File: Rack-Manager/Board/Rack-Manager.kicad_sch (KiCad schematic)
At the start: 0 parts

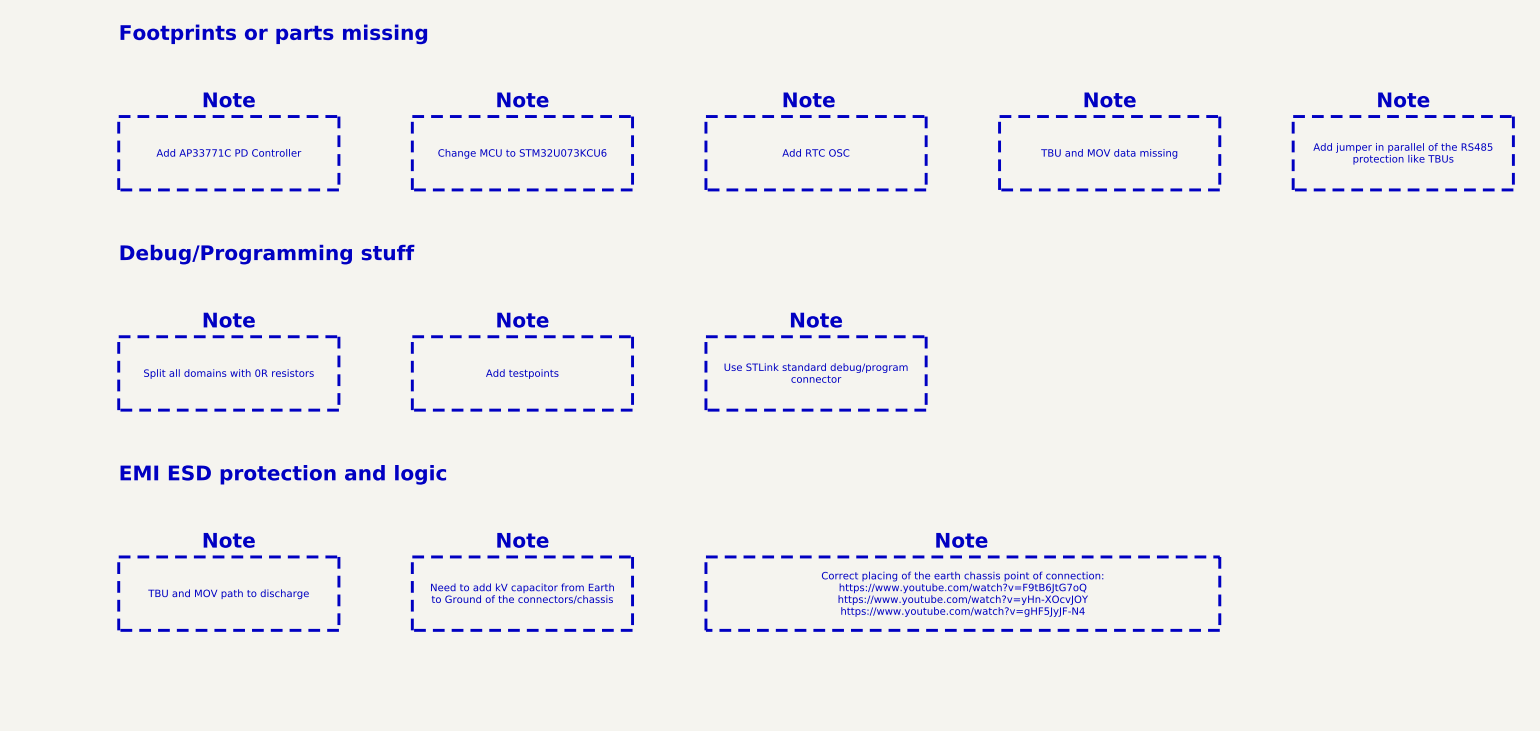
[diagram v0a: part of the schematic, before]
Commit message: Updated .gitignore, added USB-C sink controller and fix earth on GDT
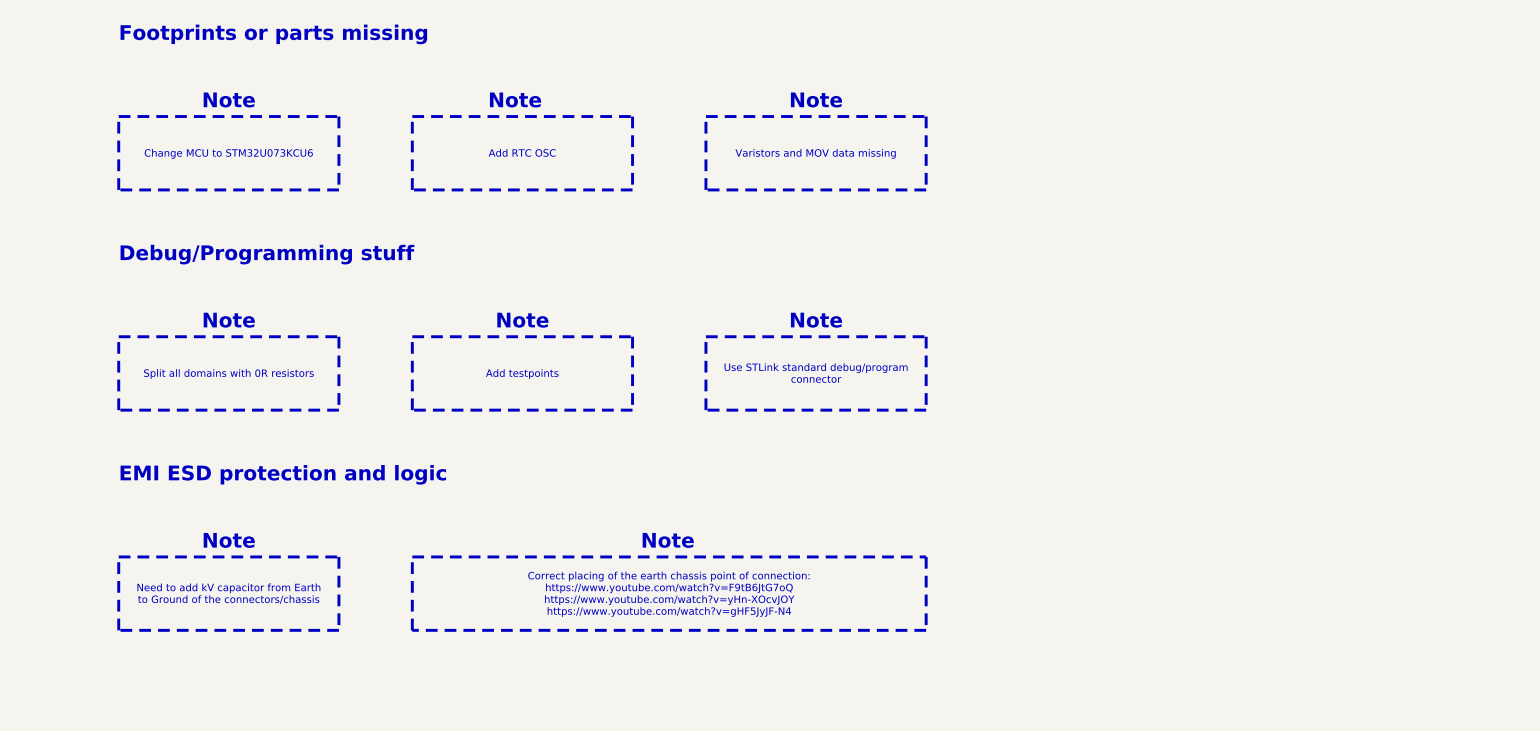
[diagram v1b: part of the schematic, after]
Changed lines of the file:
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@@
 	(text "Note"
 		(exclude_from_sim no)
-		(at 436.88 48.26 0)
-		(effects
-			(font
-				(size 2.54 2.54)
-				(thickness 0.508)
-				(bold yes)
-				(color 194 0 0 1)
-			)
-		)
-	)
-	(text "Note"
-		(exclude_from_sim no)
-		(at 387.35 124.46 0)
+		(at 386.08 48.26 0)
+		(effects
+			(font
+				(size 2.54 2.54)
+				(thickness 0.508)
+				(bold yes)
+				(color 194 0 0 1)
+			)
+		)
+	)
+	(text "Note"
+		(exclude_from_sim no)
+		(at 336.55 124.46 0)
 		(effects
 			(font
@@
 	(text "Note"
 		(exclude_from_sim no)
-		(at 488.95 48.26 0)
-		(effects
-			(font
-				(size 2.54 2.54)
-				(thickness 0.508)
-				(bold yes)
-				(color 194 0 0 1)
-			)
-		)
-	)
-	(text "Note"
-		(exclude_from_sim no)
-		(at 336.55 124.46 0)
-		(effects
-			(font
-				(size 2.54 2.54)
-				(thickness 0.508)
-				(bold yes)
-				(color 194 0 0 1)
-			)
-		)
-	)
-	(text "Note"
-		(exclude_from_sim no)
-		(at 463.296 124.46 0)
+		(at 438.15 48.26 0)
+		(effects
+			(font
+				(size 2.54 2.54)
+				(thickness 0.508)
+				(bold yes)
+				(color 194 0 0 1)
+			)
+		)
+	)
+	(text "Note"
+		(exclude_from_sim no)
+		(at 412.496 124.46 0)
 		(effects
 			(font
@@
 	(text "Note"
 		(exclude_from_sim no)
-		(at 539.75 48.26 0)
-		(effects
-			(font
-				(size 2.54 2.54)
-				(thickness 0.508)
-				(bold yes)
-				(color 194 0 0 1)
-			)
-		)
-	)
-	(text "Note"
-		(exclude_from_sim no)
 		(at 438.15 86.36 0)
 		(effects
@@
 	(text "Note"
 		(exclude_from_sim no)
-		(at 387.35 48.26 0)
-		(effects
-			(font
-				(size 2.54 2.54)
-				(thickness 0.508)
-				(bold yes)
-				(color 194 0 0 1)
-			)
-		)
-	)
-	(text "Note"
-		(exclude_from_sim no)
 		(at 387.35 86.36 0)
 		(effects
@@
 	(text_box "Need to add kV capacitor from Earth to Ground of the connectors/chassis"
 		(exclude_from_sim no)
+		(at 317.5 127 0)
+		(size 38.1 12.7)
+		(margins 0.9525 0.9525 0.9525 0.9525)
+		(stroke
+			(width 0.508)
+			(type dot)
+			(color 194 0 0 1)
+		)
+		(fill
+			(type color)
+			(color 255 165 169 1)
+		)
+		(effects
+			(font
+				(size 1.27 1.27)
+			)
+		)
+	)
+	(text_box "Split all domains with 0R resistors"
+		(exclude_from_sim no)
+		(at 317.5 88.9 0)
+		(size 38.1 12.7)
+		(margins 0.9525 0.9525 0.9525 0.9525)
+		(stroke
+			(width 0.508)
+			(type dot)
+			(color 194 0 0 1)
+		)
+		(fill
+			(type color)
+			(color 255 165 169 1)
+		)
+		(effects
+			(font
+				(size 1.27 1.27)
+			)
+		)
+	)
+	(text_box "Change MCU to STM32U073KCU6"
+		(exclude_from_sim no)
+		(at 317.5 50.8 0)
+		(size 38.1 12.7)
+		(margins 0.9525 0.9525 0.9525 0.9525)
+		(stroke
+			(width 0.508)
+			(type dot)
+			(color 194 0 0 1)
+		)
+		(fill
+			(type color)
+			(color 255 165 169 1)
+		)
+		(effects
+			(font
+				(size 1.27 1.27)
+			)
+		)
+	)
+	(text_box "Varistors and MOV data missing"
+		(exclude_from_sim no)
+		(at 419.1 50.8 0)
+		(size 38.1 12.7)
+		(margins 0.9525 0.9525 0.9525 0.9525)
+		(stroke
+			(width 0.508)
+			(type dot)
+			(color 194 0 0 1)
+		)
+		(fill
+			(type color)
+			(color 255 165 169 1)
+		)
+		(effects
+			(font
+				(size 1.27 1.27)
+			)
+		)
+	)
+	(text_box "Add RTC OSC"
+		(exclude_from_sim no)
+		(at 368.3 50.8 0)
+		(size 38.1 12.7)
+		(margins 0.9525 0.9525 0.9525 0.9525)
+		(stroke
+			(width 0.508)
+			(type dot)
+			(color 194 0 0 1)
+		)
+		(fill
+			(type color)
+			(color 255 165 169 1)
+		)
+		(effects
+			(font
+				(size 1.27 1.27)
+			)
+		)
+	)
+	(text_box "Use STLink standard debug/program connector"
+		(exclude_from_sim no)
+		(at 419.1 88.9 0)
+		(size 38.1 12.7)
+		(margins 0.9525 0.9525 0.9525 0.9525)
+		(stroke
+			(width 0.508)
+			(type dot)
+			(color 194 0 0 1)
+		)
+		(fill
+			(type color)
+			(color 255 165 169 1)
+		)
+		(effects
+			(font
+				(size 1.27 1.27)
+			)
+		)
+	)
+	(text_box "Add testpoints"
+		(exclude_from_sim no)
+		(at 368.3 88.9 0)
+		(size 38.1 12.7)
+		(margins 0.9525 0.9525 0.9525 0.9525)
+		(stroke
+			(width 0.508)
+			(type dot)
+			(color 194 0 0 1)
+		)
+		(fill
+			(type color)
+			(color 255 165 169 1)
+		)
+		(effects
+			(font
+				(size 1.27 1.27)
+			)
+		)
+	)
+	(text_box "Correct placing of the earth chassis point of connection:\nhttps://www.youtube.com/watch?v=F9tB6JtG7oQ\nhttps://www.youtube.com/watch?v=yHn-XOcvJOY\nhttps://www.youtube.com/watch?v=gHF5JyJF-N4"
+		(exclude_from_sim no)
 		(at 368.3 127 0)
-		(size 38.1 12.7)
-		(margins 0.9525 0.9525 0.9525 0.9525)
-		(stroke
-			(width 0.508)
-			(type dot)
-			(color 194 0 0 1)
-		)
-		(fill
-			(type color)
-			(color 255 165 169 1)
-		)
-		(effects
-			(font
-				(size 1.27 1.27)
-			)
-		)
-	)
-	(text_box "Add jumper in parallel of the RS485 protection like TBUs"
-		(exclude_from_sim no)
-		(at 520.7 50.8 0)
-		(size 38.1 12.7)
-		(margins 0.9525 0.9525 0.9525 0.9525)
-		(stroke
-			(width 0.508)
-			(type dot)
-			(color 194 0 0 1)
-		)
-		(fill
-			(type color)
-			(color 255 165 169 1)
-		)
-		(effects
-			(font
-				(size 1.27 1.27)
-			)
-		)
-	)
-	(text_box "Split all domains with 0R resistors"
-		(exclude_from_sim no)
-		(at 317.5 88.9 0)
-		(size 38.1 12.7)
-		(margins 0.9525 0.9525 0.9525 0.9525)
-		(stroke
-			(width 0.508)
-			(type dot)
-			(color 194 0 0 1)
-		)
-		(fill
-			(type color)
-			(color 255 165 169 1)
-		)
-		(effects
-			(font
-				(size 1.27 1.27)
-			)
-		)
-	)
-	(text_box "Change MCU to STM32U073KCU6"
-		(exclude_from_sim no)
-		(at 368.3 50.8 0)
-		(size 38.1 12.7)
-		(margins 0.9525 0.9525 0.9525 0.9525)
-		(stroke
-			(width 0.508)
-			(type dot)
-			(color 194 0 0 1)
-		)
-		(fill
-			(type color)
-			(color 255 165 169 1)
-		)
-		(effects
-			(font
-				(size 1.27 1.27)
-			)
-		)
-	)
-	(text_box "TBU and MOV path to discharge"
-		(exclude_from_sim no)
-		(at 317.5 127 0)
-		(size 38.1 12.7)
-		(margins 0.9525 0.9525 0.9525 0.9525)
-		(stroke
-			(width 0.508)
-			(type dot)
-			(color 194 0 0 1)
-		)
-		(fill
-			(type color)
-			(color 255 165 169 1)
-		)
-		(effects
-			(font
-				(size 1.27 1.27)
-			)
-		)
-	)
-	(text_box "TBU and MOV data missing"
-		(exclude_from_sim no)
-		(at 469.9 50.8 0)
-		(size 38.1 12.7)
-		(margins 0.9525 0.9525 0.9525 0.9525)
-		(stroke
-			(width 0.508)
-			(type dot)
-			(color 194 0 0 1)
-		)
-		(fill
-			(type color)
-			(color 255 165 169 1)
-		)
-		(effects
-			(font
-				(size 1.27 1.27)
-			)
-		)
-	)
-	(text_box "Add RTC OSC"
-		(exclude_from_sim no)
-		(at 419.1 50.8 0)
-		(size 38.1 12.7)
-		(margins 0.9525 0.9525 0.9525 0.9525)
-		(stroke
-			(width 0.508)
-			(type dot)
-			(color 194 0 0 1)
-		)
-		(fill
-			(type color)
-			(color 255 165 169 1)
-		)
-		(effects
-			(font
-				(size 1.27 1.27)
-			)
-		)
-	)
-	(text_box "Add AP33771C PD Controller"
-		(exclude_from_sim no)
-		(at 317.5 50.8 0)
-		(size 38.1 12.7)
-		(margins 0.9525 0.9525 0.9525 0.9525)
-		(stroke
-			(width 0.508)
-			(type dot)
-			(color 194 0 0 1)
-		)
-		(fill
-			(type color)
-			(color 255 165 169 1)
-		)
-		(effects
-			(font
-				(size 1.27 1.27)
-			)
-		)
-	)
-	(text_box "Use STLink standard debug/program connector"
-		(exclude_from_sim no)
-		(at 419.1 88.9 0)
-		(size 38.1 12.7)
-		(margins 0.9525 0.9525 0.9525 0.9525)
-		(stroke
-			(width 0.508)
-			(type dot)
-			(color 194 0 0 1)
-		)
-		(fill
-			(type color)
-			(color 255 165 169 1)
-		)
-		(effects
-			(font
-				(size 1.27 1.27)
-			)
-		)
-	)
-	(text_box "Add testpoints"
-		(exclude_from_sim no)
-		(at 368.3 88.9 0)
-		(size 38.1 12.7)
-		(margins 0.9525 0.9525 0.9525 0.9525)
-		(stroke
-			(width 0.508)
-			(type dot)
-			(color 194 0 0 1)
-		)
-		(fill
-			(type color)
-			(color 255 165 169 1)
-		)
-		(effects
-			(font
-				(size 1.27 1.27)
-			)
-		)
-	)
-	(text_box "Correct placing of the earth chassis point of connection:\nhttps://www.youtube.com/watch?v=F9tB6JtG7oQ\nhttps://www.youtube.com/watch?v=yHn-XOcvJOY\nhttps://www.youtube.com/watch?v=gHF5JyJF-N4"
-		(exclude_from_sim no)
-		(at 419.1 127 0)
 		(size 88.9 12.7)
 		(margins 0.9525 0.9525 0.9525 0.9525)

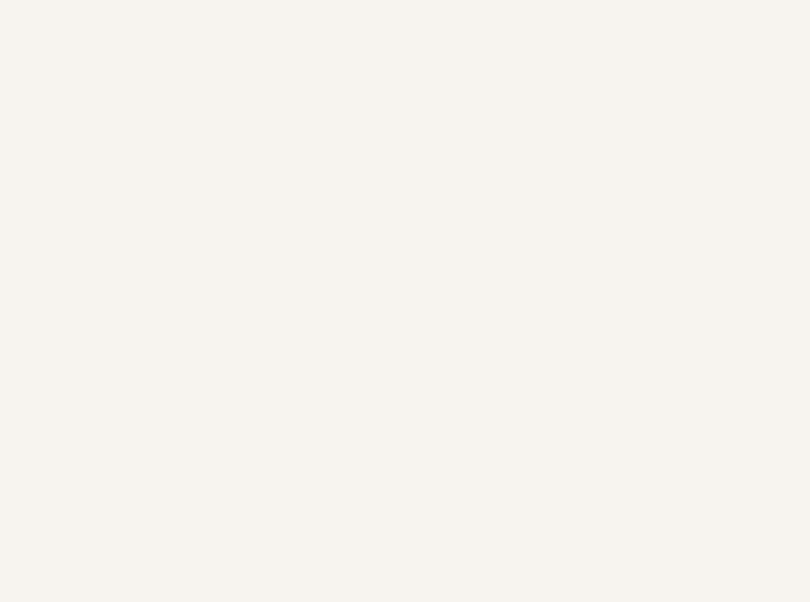
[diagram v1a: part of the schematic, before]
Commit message: Added the fan management sheet and the mosfets for it
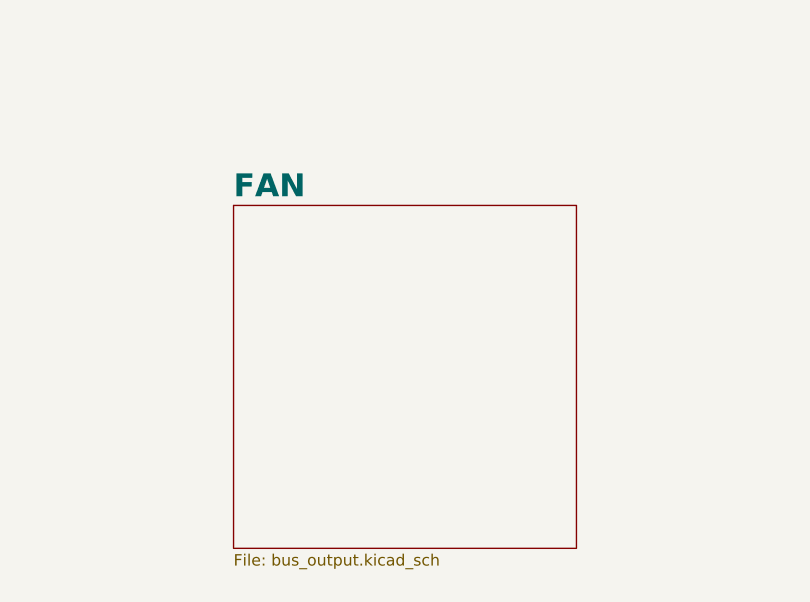
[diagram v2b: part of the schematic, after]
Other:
- added sheet FAN (bus_output.kicad_sch)
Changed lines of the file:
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@@
+	)
+	(sheet
+		(at 229.87 113.03)
+		(size 38.1 38.1)
+		(exclude_from_sim no)
+		(in_bom yes)
+		(on_board yes)
+		(dnp no)
+		(fields_autoplaced yes)
+		(stroke
+			(width 0.1524)
+			(type solid)
+		)
+		(fill
+			(color 255 255 194 1.0000)
+		)
+		(property "Sheetname" "FAN"
+			(at 229.87 112.3184 0)
+			(effects
+				(font
+					(size 2.54 2.54)
+					(thickness 0.508)
+					(bold yes)
+				)
+				(justify left bottom)
+			)
+		)
+		(property "Sheetfile" "bus_output.kicad_sch"
+			(at 229.87 151.7146 0)
+			(effects
+				(font
+					(size 1.27 1.27)
+				)
+				(justify left top)
+			)
+		)
+		(instances
+			(project "Rack-Manager"
+				(path "/5d42174d-da49-4bca-870b-353868af7168"
+					(page "9")
+				)
+			)
+		)
 	)
 	(sheet

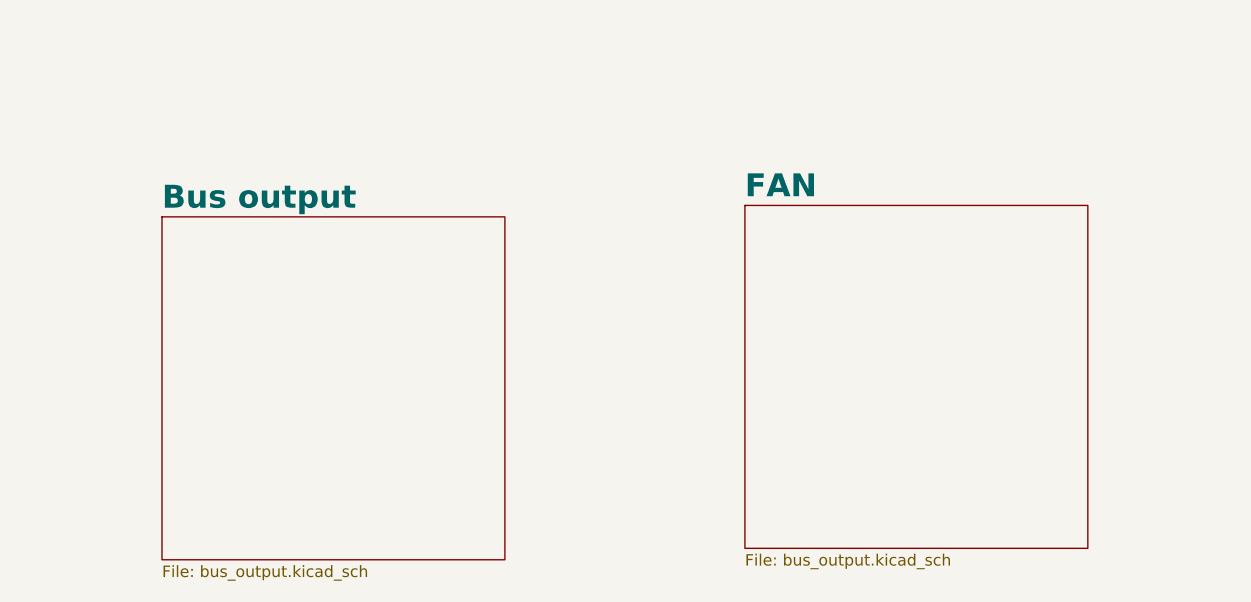
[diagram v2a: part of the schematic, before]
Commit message: Created dedicated FAN file
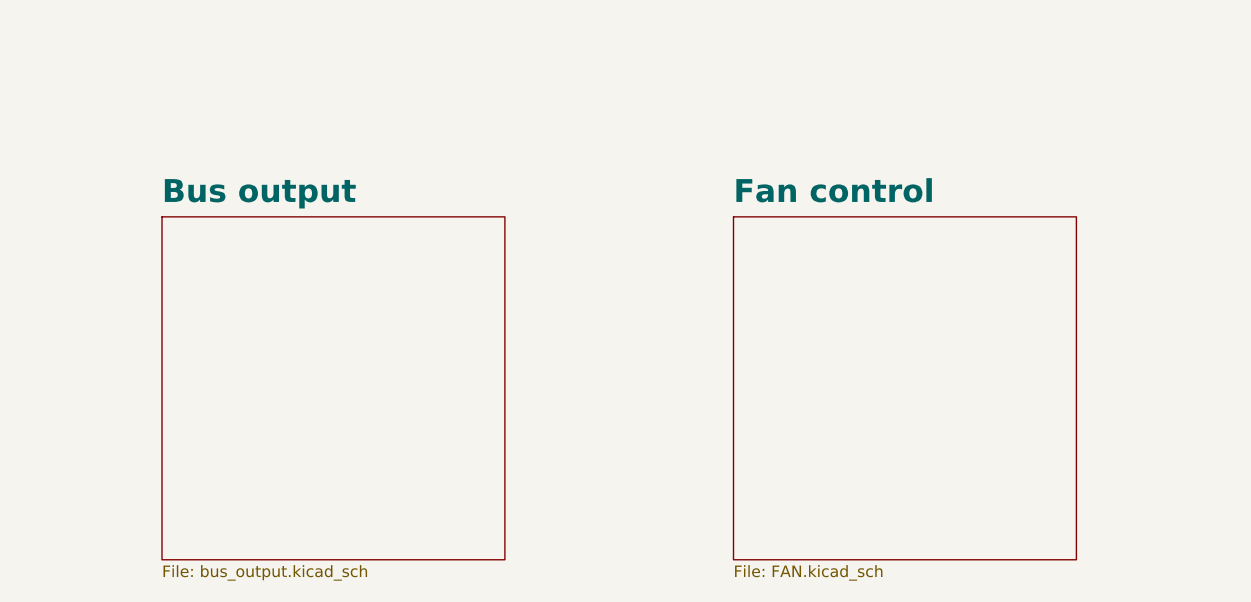
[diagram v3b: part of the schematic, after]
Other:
- removed sheet FAN
- added sheet Fan control (FAN.kicad_sch)
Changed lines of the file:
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@@
+	)
+	(sheet
+		(at 228.6 114.3)
+		(size 38.1 38.1)
+		(exclude_from_sim no)
+		(in_bom yes)
+		(on_board yes)
+		(dnp no)
+		(fields_autoplaced yes)
+		(stroke
+			(width 0.1524)
+			(type solid)
+		)
+		(fill
+			(color 255 255 194 1.0000)
+		)
+		(property "Sheetname" "Fan control"
+			(at 228.6 112.9534 0)
+			(effects
+				(font
+					(size 2.54 2.54)
+					(thickness 0.508)
+					(bold yes)
+				)
+				(justify left bottom)
+			)
+		)
+		(property "Sheetfile" "FAN.kicad_sch"
+			(at 228.6 152.9846 0)
+			(effects
+				(font
+					(size 1.27 1.27)
+				)
+				(justify left top)
+			)
+		)
+		(instances
+			(project "Rack-Manager"
+				(path "/5d42174d-da49-4bca-870b-353868af7168"
+					(page "10")
+				)
+			)
+		)
 	)
 	(sheet
@@
 		)
 		(property "Sheetname" "Bus output"
-			(at 165.1 113.5884 0)
+			(at 165.1 112.9534 0)
 			(effects
 				(font
@@
 				)
 			)
-		)
-	)
-	(sheet
-		(at 229.87 113.03)
-		(size 38.1 38.1)
-		(exclude_from_sim no)
-		(in_bom yes)
-		(on_board yes)
-		(dnp no)
-		(fields_autoplaced yes)
-		(stroke
-			(width 0.1524)
-			(type solid)
-		)
-		(fill
-			(color 255 255 194 1.0000)
-		)
-		(property "Sheetname" "FAN"
-			(at 229.87 112.3184 0)
-			(effects
-				(font
-					(size 2.54 2.54)
-					(thickness 0.508)
-					(bold yes)
-				)
-				(justify left bottom)
-			)
-		)
-		(property "Sheetfile" "bus_output.kicad_sch"
-			(at 229.87 151.7146 0)
-			(effects
-				(font
-					(size 1.27 1.27)
-				)
-				(justify left top)
-			)
-		)
-		(instances
-			(project "Rack-Manager"
-				(path "/5d42174d-da49-4bca-870b-353868af7168"
-					(page "9")
-				)
-			)

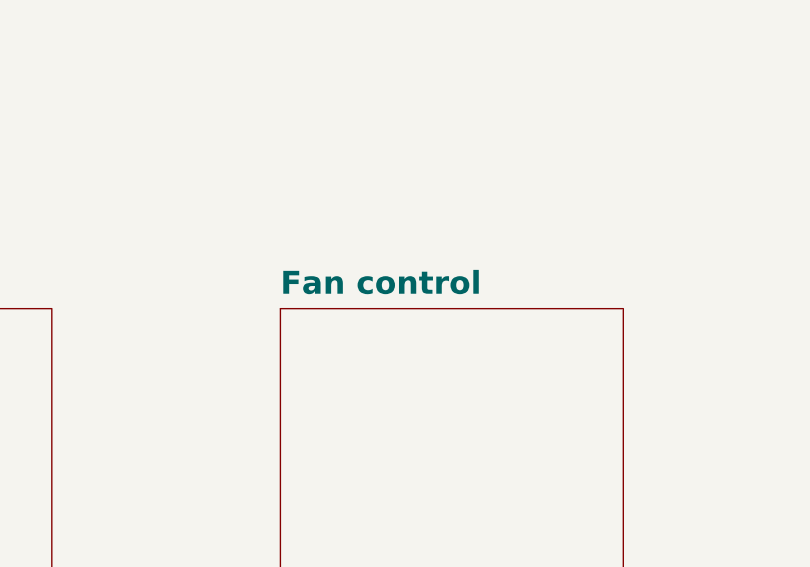
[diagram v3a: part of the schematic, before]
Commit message: Fixed FAN control link mixed with bus output file
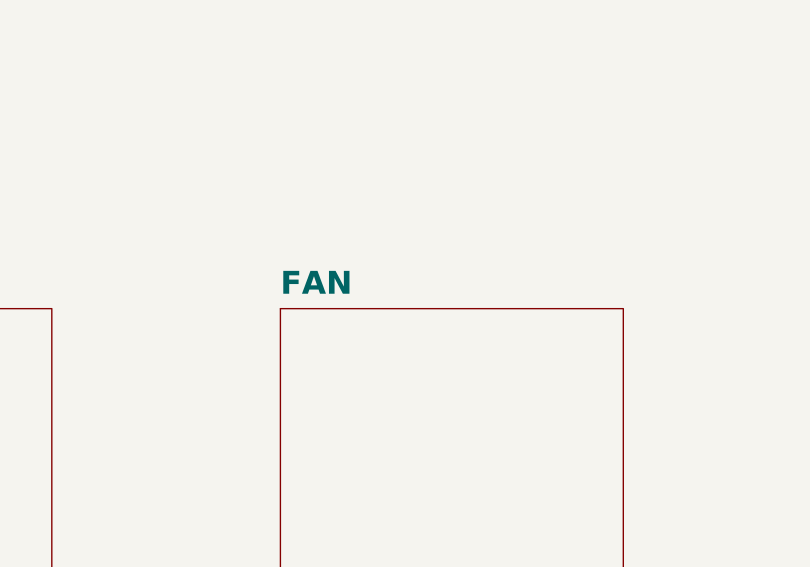
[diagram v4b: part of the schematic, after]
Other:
- sheet Fan control renamed FAN
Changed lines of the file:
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@@
 			(color 255 255 194 1.0000)
 		)
-		(property "Sheetname" "Fan control"
+		(property "Sheetname" "FAN"
 			(at 228.6 112.9534 0)
 			(effects
